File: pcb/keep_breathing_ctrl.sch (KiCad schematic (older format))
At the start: 4 parts

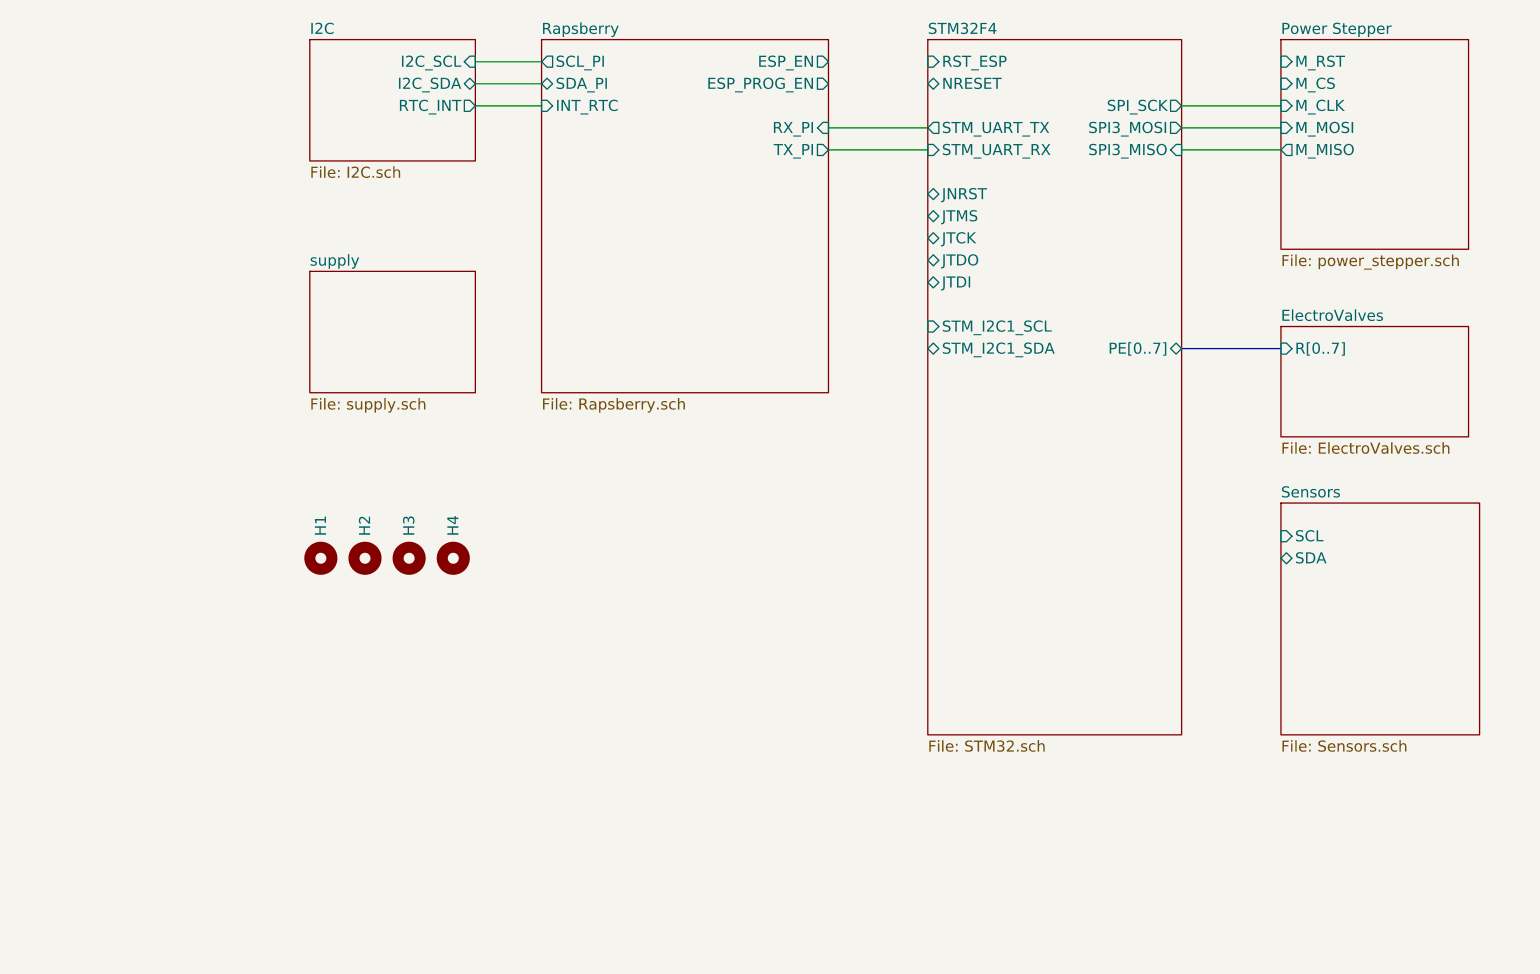
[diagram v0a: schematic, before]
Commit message: sensor array started
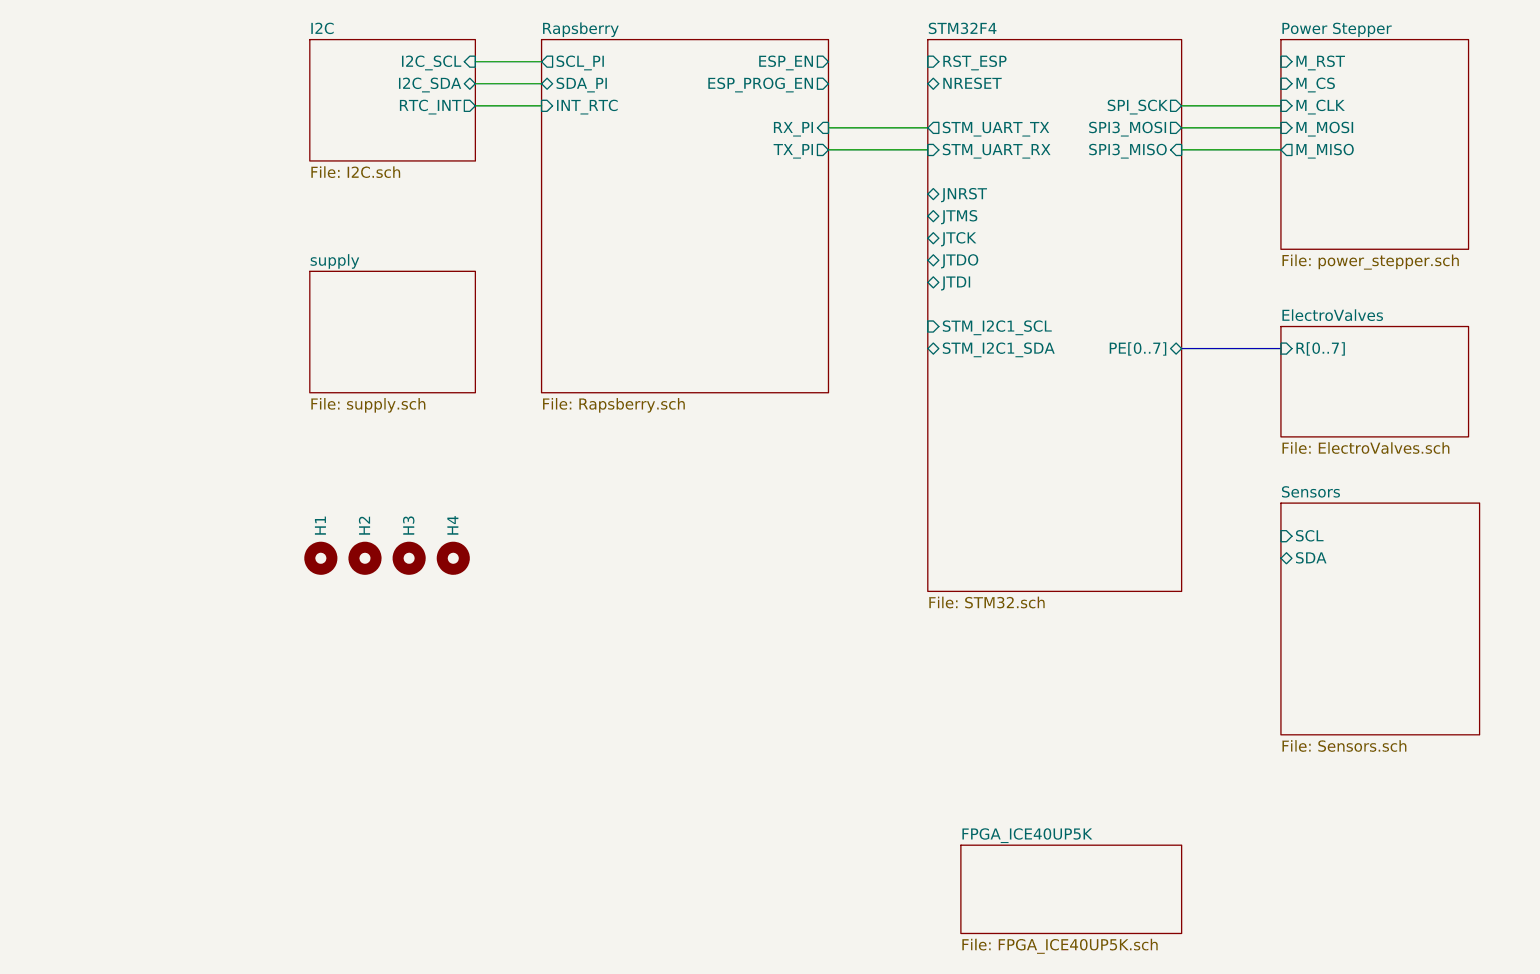
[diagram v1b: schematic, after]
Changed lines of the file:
@@
 $Descr A4 11693 8268
 encoding utf-8
-Sheet 1 8
+Sheet 1 18
 Title ""
 Date ""
@@
 	4200 2450 4500 2450
 $Sheet
-S 6250 2150 1150 3150
+S 6250 2150 1150 2500
 U 5E989259
 F0 "STM32F4" 50
@@
 F3 "SDA" B L 7850 4500 50
 $EndSheet
+$Sheet
+S 6400 5800 1000 400
+U 5E9B245C
+F0 "FPGA_ICE40UP5K" 50
+F1 "FPGA_ICE40UP5K.sch" 50
+$EndSheet
 $EndSCHEMATC

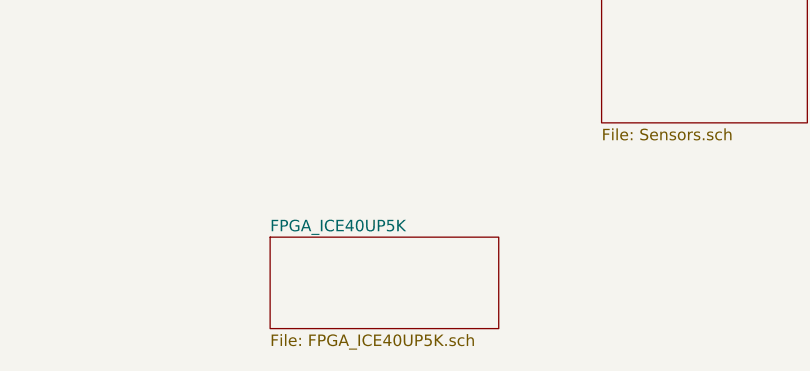
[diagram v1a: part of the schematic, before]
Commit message: array sensor improved
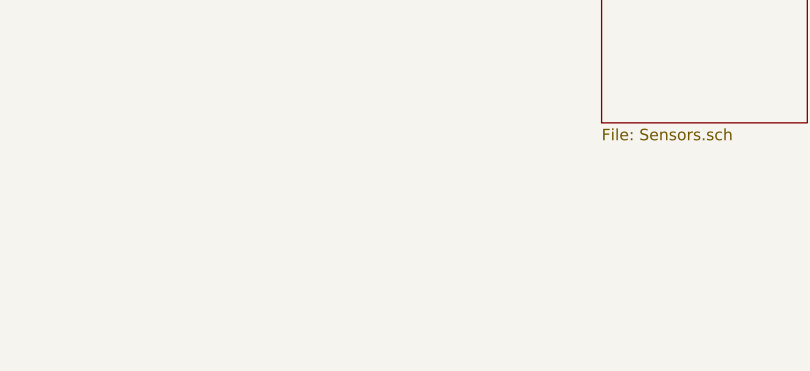
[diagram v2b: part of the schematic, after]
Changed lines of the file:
@@
 $Descr A4 11693 8268
 encoding utf-8
-Sheet 1 18
+Sheet 1 9
 Title ""
 Date ""
@@
 F3 "SDA" B L 7850 4500 50
 $EndSheet
-$Sheet
-S 6400 5800 1000 400
-U 5E9B245C
-F0 "FPGA_ICE40UP5K" 50
-F1 "FPGA_ICE40UP5K.sch" 50
-$EndSheet
 $EndSCHEMATC

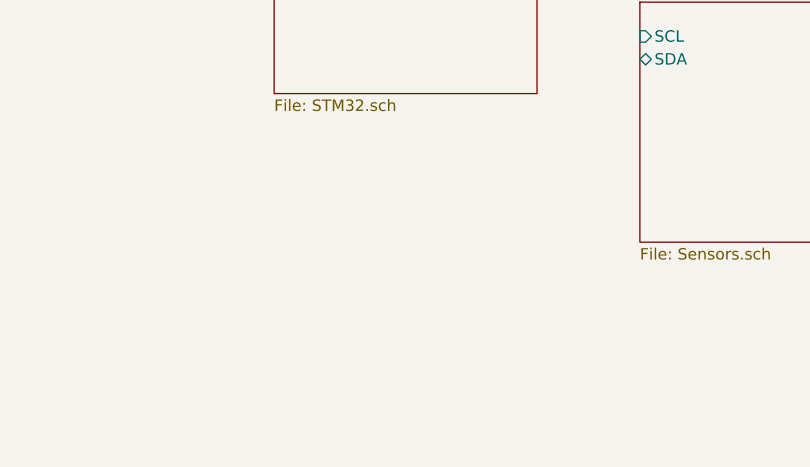
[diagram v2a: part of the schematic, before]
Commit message: schematic simplified
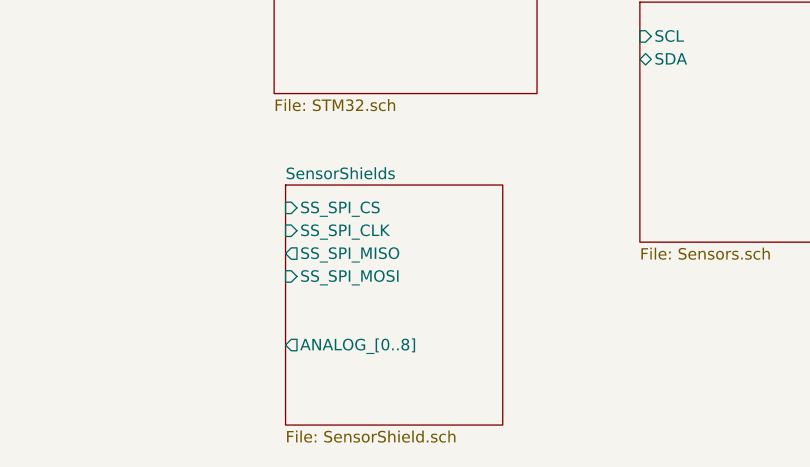
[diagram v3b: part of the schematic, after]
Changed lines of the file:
@@
 F3 "SDA" B L 7850 4500 50
 $EndSheet
+$Sheet
+S 6300 5050 950  1050
+U 5E9C016D
+F0 "SensorShields" 50
+F1 "SensorShield.sch" 50
+F2 "SS_SPI_CS" I L 6300 5150 50
+F3 "SS_SPI_CLK" I L 6300 5250 50
+F4 "SS_SPI_MISO" O L 6300 5350 50
+F5 "SS_SPI_MOSI" I L 6300 5450 50
+F6 "ANALOG_[0..8]" O L 6300 5750 50
+$EndSheet
 $EndSCHEMATC

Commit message: fix
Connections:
- wire segments 8 -> 13
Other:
- moved on the sheet: H1, H2, H3, H4
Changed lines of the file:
@@
 L Mechanical:MountingHole H1
 U 1 1 5E9C23FB
-P 3500 4500
-F 0 "H1" H 3600 4500 50  0000 L CNN
-F 1 "MountingHole" H 3600 4455 50  0001 L CNN
-F 2 "MountingHole:MountingHole_2.7mm_M2.5" H 3500 4500 50  0001 C CNN
-F 3 "~" H 3500 4500 50  0001 C CNN
-	1    3500 4500
+P 2200 4400
+F 0 "H1" H 2300 4400 50  0000 L CNN
+F 1 "MountingHole" H 2300 4355 50  0001 L CNN
+F 2 "MountingHole:MountingHole_2.7mm_M2.5" H 2200 4400 50  0001 C CNN
+F 3 "~" H 2200 4400 50  0001 C CNN
+	1    2200 4400
 	0    -1   -1   0
 $EndComp
@@
 L Mechanical:MountingHole H2
 U 1 1 5E9C36D2
-P 3700 4500
-F 0 "H2" H 3800 4500 50  0000 L CNN
-F 1 "MountingHole" H 3800 4455 50  0001 L CNN
-F 2 "MountingHole:MountingHole_2.7mm_M2.5" H 3700 4500 50  0001 C CNN
-F 3 "~" H 3700 4500 50  0001 C CNN
-	1    3700 4500
+P 2400 4400
+F 0 "H2" H 2500 4400 50  0000 L CNN
+F 1 "MountingHole" H 2500 4355 50  0001 L CNN
+F 2 "MountingHole:MountingHole_2.7mm_M2.5" H 2400 4400 50  0001 C CNN
+F 3 "~" H 2400 4400 50  0001 C CNN
+	1    2400 4400
 	0    -1   -1   0
 $EndComp
@@
 L Mechanical:MountingHole H3
 U 1 1 5E9C5DAB
-P 3900 4500
-F 0 "H3" H 4000 4500 50  0000 L CNN
-F 1 "MountingHole" H 4000 4455 50  0001 L CNN
-F 2 "MountingHole:MountingHole_2.7mm_M2.5" H 3900 4500 50  0001 C CNN
-F 3 "~" H 3900 4500 50  0001 C CNN
-	1    3900 4500
+P 2600 4400
+F 0 "H3" H 2700 4400 50  0000 L CNN
+F 1 "MountingHole" H 2700 4355 50  0001 L CNN
+F 2 "MountingHole:MountingHole_2.7mm_M2.5" H 2600 4400 50  0001 C CNN
+F 3 "~" H 2600 4400 50  0001 C CNN
+	1    2600 4400
 	0    -1   -1   0
 $EndComp
@@
 L Mechanical:MountingHole H4
 U 1 1 5E9C5DB5
-P 4100 4500
-F 0 "H4" H 4200 4500 50  0000 L CNN
-F 1 "MountingHole" H 4200 4455 50  0001 L CNN
-F 2 "MountingHole:MountingHole_2.7mm_M2.5" H 4100 4500 50  0001 C CNN
-F 3 "~" H 4100 4500 50  0001 C CNN
-	1    4100 4500
+P 2800 4400
+F 0 "H4" H 2900 4400 50  0000 L CNN
+F 1 "MountingHole" H 2900 4355 50  0001 L CNN
+F 2 "MountingHole:MountingHole_2.7mm_M2.5" H 2800 4400 50  0001 C CNN
+F 3 "~" H 2800 4400 50  0001 C CNN
+	1    2800 4400
 	0    -1   -1   0
 $EndComp
 $Sheet
-S 3450 3200 750  550
+S 2500 3050 750  550
 U 5E8E60A3
 F0 "supply" 50
@@
 $EndSheet
 $Sheet
-S 3450 2150 750  550
-U 5E8F4152
-F0 "I2C" 50
-F1 "I2C.sch" 50
-F2 "I2C_SDA" B R 4200 2350 50
-F3 "I2C_SCL" I R 4200 2250 50
-F4 "RTC_INT" O R 4200 2450 50
-$EndSheet
-$Sheet
-S 4500 2150 1300 1600
+S 4100 2150 1700 1600
 U 5E96F696
 F0 "Rapsberry" 50
@@
 F4 "ESP_PROG_EN" O R 5800 2350 50
 F5 "ESP_EN" O R 5800 2250 50
-F6 "SDA_PI" B L 4500 2350 50
-F7 "SCL_PI" O L 4500 2250 50
-F8 "INT_RTC" I L 4500 2450 50
+F6 "SDA_PI" B L 4100 2350 50
+F7 "SCL_PI" O L 4100 2250 50
+F8 "INT_RTC" I L 4100 2450 50
 $EndSheet
 Wire Wire Line
@@
 	5800 2650 6250 2650
 Wire Wire Line
-	4200 2250 4500 2250
+	3800 2250 4100 2250
 Wire Wire Line
-	4200 2350 4500 2350
+	3800 2350 4100 2350
 Wire Wire Line
-	4200 2450 4500 2450
+	3800 2450 4100 2450
 $Sheet
-S 6250 2150 1150 2500
+S 6250 2150 1150 3100
 U 5E989259
 F0 "STM32F4" 50
@@
 F13 "SPI3_MOSI" O R 7400 2550 50
 F14 "SPI3_MISO" I R 7400 2650 50
-F15 "SPI_SCK" O R 7400 2450 50
-F16 "PE[0..7]" B R 7400 3550 50
+F15 "PE[0..7]" B R 7400 3550 50
+F16 "SEN[0..8]" I L 6250 4450 50
+F17 "SPI3_SCK" O R 7400 2450 50
 $EndSheet
 Wire Wire Line
@@
 $EndSheet
 $Sheet
-S 6300 5050 950  1050
+S 4100 4100 1700 1100
 U 5E9C016D
 F0 "SensorShields" 50
 F1 "SensorShield.sch" 50
-F2 "SS_SPI_CS" I L 6300 5150 50
-F3 "SS_SPI_CLK" I L 6300 5250 50
-F4 "SS_SPI_MISO" O L 6300 5350 50
-F5 "SS_SPI_MOSI" I L 6300 5450 50
-F6 "ANALOG_[0..8]" O L 6300 5750 50
+F2 "SS_SPI_CS" I R 5800 4700 50
+F3 "SS_SPI_CLK" I R 5800 4800 50
+F4 "SS_SPI_MISO" O R 5800 5000 50
+F5 "SS_SPI_MOSI" I R 5800 4900 50
+F6 "ANALOG_[0..8]" O R 5800 4450 50
+$EndSheet
+Wire Bus Line
+	5800 4450 6250 4450
+Wire Wire Line
+	5800 4700 5800 4800
+Wire Wire Line
+	5800 4800 6250 4800
+Wire Wire Line
+	5800 4700 6250 4700
+Wire Wire Line
+	5800 4900 6250 4900
+Wire Wire Line
+	5800 5000 6250 5000
+$Sheet
+S 3050 2150 750  550
+U 5E8F4152
+F0 "I2C" 50
+F1 "I2C.sch" 50
+F2 "I2C_SDA" B R 3800 2350 50
+F3 "I2C_SCL" I R 3800 2250 50
+F4 "RTC_INT" O R 3800 2450 50
 $EndSheet
 $EndSCHEMATC

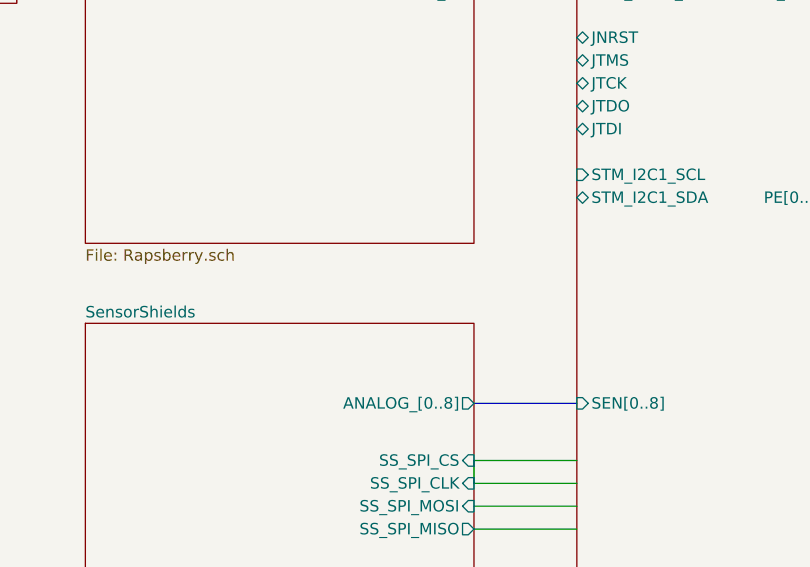
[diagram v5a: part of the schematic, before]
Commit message: SPI connections between FPGA, PI and FLASH
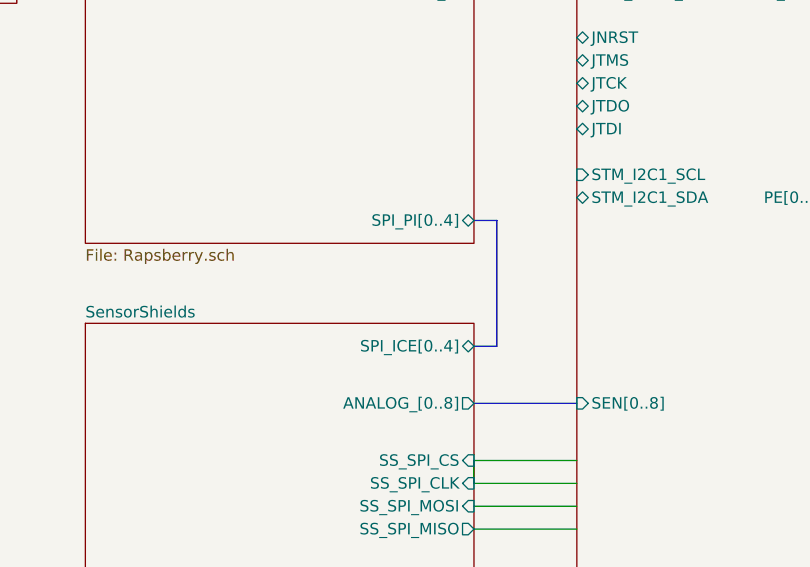
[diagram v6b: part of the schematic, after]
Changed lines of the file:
@@
 F7 "SCL_PI" O L 4100 2250 50
 F8 "INT_RTC" I L 4100 2450 50
+F9 "SPI_PI[0..4]" B R 5800 3650 50
 $EndSheet
 Wire Wire Line
@@
 F5 "SS_SPI_MOSI" I R 5800 4900 50
 F6 "ANALOG_[0..8]" O R 5800 4450 50
+F7 "SPI_ICE[0..4]" B R 5800 4200 50
 $EndSheet
 Wire Bus Line
@@
 F4 "RTC_INT" O R 3800 2450 50
 $EndSheet
+Wire Bus Line
+	5800 3650 5900 3650
+Wire Bus Line
+	5900 3650 5900 4200
+Wire Bus Line
+	5900 4200 5800 4200
 $EndSCHEMATC

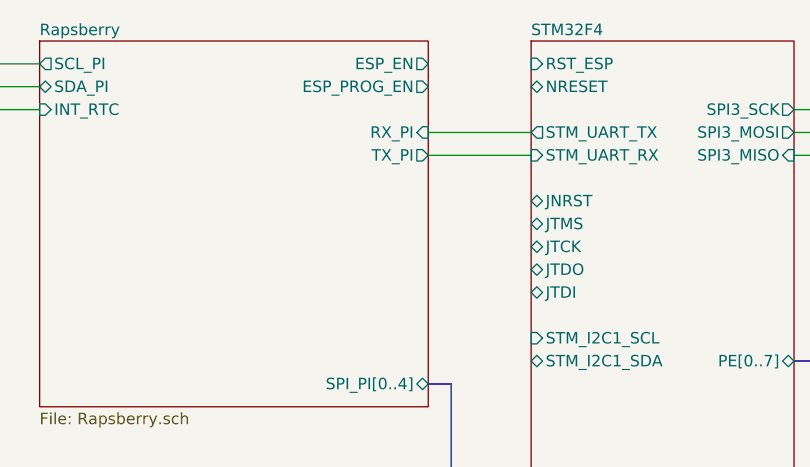
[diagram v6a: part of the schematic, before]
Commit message: stm32 jtag  connected
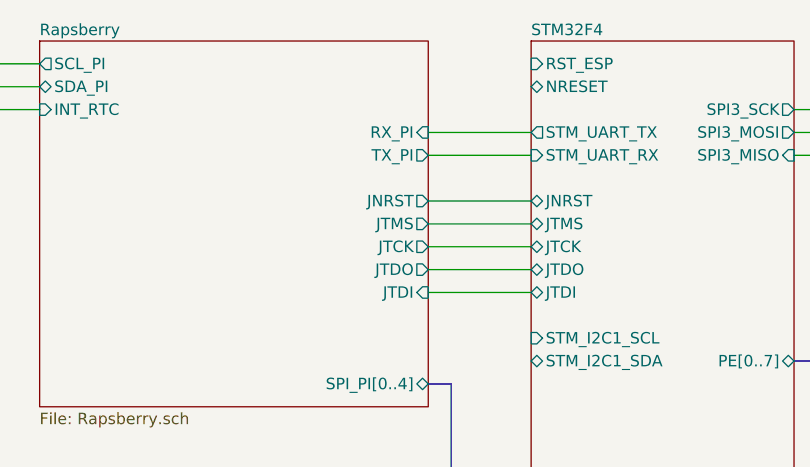
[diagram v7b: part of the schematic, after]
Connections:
- wire segments 13 -> 18
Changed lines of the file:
@@
 EESchema Schematic File Version 4
+LIBS:keep_breathing_ctrl-cache
 EELAYER 30 0
 EELAYER END
@@
 F1 "supply.sch" 50
 $EndSheet
-$Sheet
-S 4100 2150 1700 1600
-U 5E96F696
-F0 "Rapsberry" 50
-F1 "Rapsberry.sch" 50
-F2 "TX_PI" O R 5800 2650 50
-F3 "RX_PI" I R 5800 2550 50
-F4 "ESP_PROG_EN" O R 5800 2350 50
-F5 "ESP_EN" O R 5800 2250 50
-F6 "SDA_PI" B L 4100 2350 50
-F7 "SCL_PI" O L 4100 2250 50
-F8 "INT_RTC" I L 4100 2450 50
-F9 "SPI_PI[0..4]" B R 5800 3650 50
-$EndSheet
 Wire Wire Line
 	5800 2550 6250 2550
@@
 Wire Wire Line
 	3800 2450 4100 2450
-$Sheet
-S 6250 2150 1150 3100
-U 5E989259
-F0 "STM32F4" 50
-F1 "STM32.sch" 50
-F2 "JNRST" B L 6250 2850 50
-F3 "JTMS" B L 6250 2950 50
-F4 "JTCK" B L 6250 3050 50
-F5 "JTDO" B L 6250 3150 50
-F6 "JTDI" B L 6250 3250 50
-F7 "NRESET" B L 6250 2350 50
-F8 "STM_I2C1_SCL" I L 6250 3450 50
-F9 "STM_I2C1_SDA" B L 6250 3550 50
-F10 "RST_ESP" I L 6250 2250 50
-F11 "STM_UART_TX" O L 6250 2550 50
-F12 "STM_UART_RX" I L 6250 2650 50
-F13 "SPI3_MOSI" O R 7400 2550 50
-F14 "SPI3_MISO" I R 7400 2650 50
-F15 "PE[0..7]" B R 7400 3550 50
-F16 "SEN[0..8]" I L 6250 4450 50
-F17 "SPI3_SCK" O R 7400 2450 50
-$EndSheet
 Wire Wire Line
 	7400 2450 7850 2450
@@
 Wire Bus Line
 	5900 4200 5800 4200
+Wire Wire Line
+	6250 2850 5800 2850
+Wire Wire Line
+	6250 2950 5800 2950
+Wire Wire Line
+	6250 3050 5800 3050
+Wire Wire Line
+	6250 3150 5800 3150
+Wire Wire Line
+	6250 3250 5800 3250
+$Sheet
+S 6250 2150 1150 3100
+U 5E989259
+F0 "STM32F4" 50
+F1 "STM32.sch" 50
+F2 "JNRST" B L 6250 2850 50
+F3 "JTMS" B L 6250 2950 50
+F4 "JTCK" B L 6250 3050 50
+F5 "JTDO" B L 6250 3150 50
+F6 "JTDI" B L 6250 3250 50
+F7 "NRESET" B L 6250 2350 50
+F8 "STM_I2C1_SCL" I L 6250 3450 50
+F9 "STM_I2C1_SDA" B L 6250 3550 50
+F10 "RST_ESP" I L 6250 2250 50
+F11 "STM_UART_TX" O L 6250 2550 50
+F12 "STM_UART_RX" I L 6250 2650 50
+F13 "SPI3_MOSI" O R 7400 2550 50
+F14 "SPI3_MISO" I R 7400 2650 50
+F15 "PE[0..7]" B R 7400 3550 50
+F16 "SEN[0..8]" I L 6250 4450 50
+F17 "SPI3_SCK" O R 7400 2450 50
+$EndSheet
+$Sheet
+S 4100 2150 1700 1600
+U 5E96F696
+F0 "Rapsberry" 50
+F1 "Rapsberry.sch" 50
+F2 "TX_PI" O R 5800 2650 50
+F3 "RX_PI" I R 5800 2550 50
+F4 "SDA_PI" B L 4100 2350 50
+F5 "SCL_PI" O L 4100 2250 50
+F6 "INT_RTC" I L 4100 2450 50
+F7 "SPI_PI[0..4]" B R 5800 3650 50
+F8 "JTMS" O R 5800 2950 50
+F9 "JTCK" O R 5800 3050 50
+F10 "JTDI" I R 5800 3250 50
+F11 "JNRST" O R 5800 2850 50
+F12 "JTDO" O R 5800 3150 50
+$EndSheet
 $EndSCHEMATC

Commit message: replacement
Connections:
- wire segments 18 -> 20
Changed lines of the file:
@@
 F12 "JTDO" O R 5800 3150 50
 $EndSheet
+Wire Wire Line
+	7850 2250 7400 2250
+Wire Wire Line
+	7850 2350 7400 2350
 $EndSCHEMATC
